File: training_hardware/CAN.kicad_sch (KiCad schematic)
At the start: 7 parts, among them U3 OKI

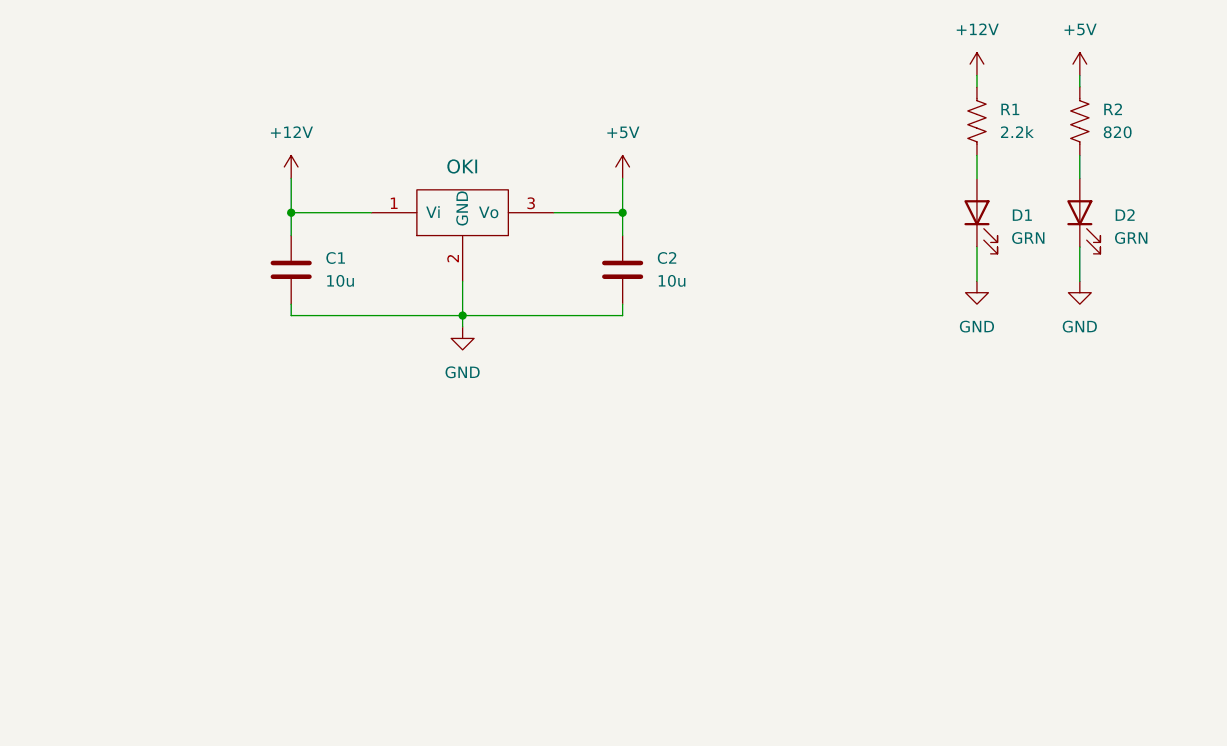
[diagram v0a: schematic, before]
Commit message: Add CAN Transciever
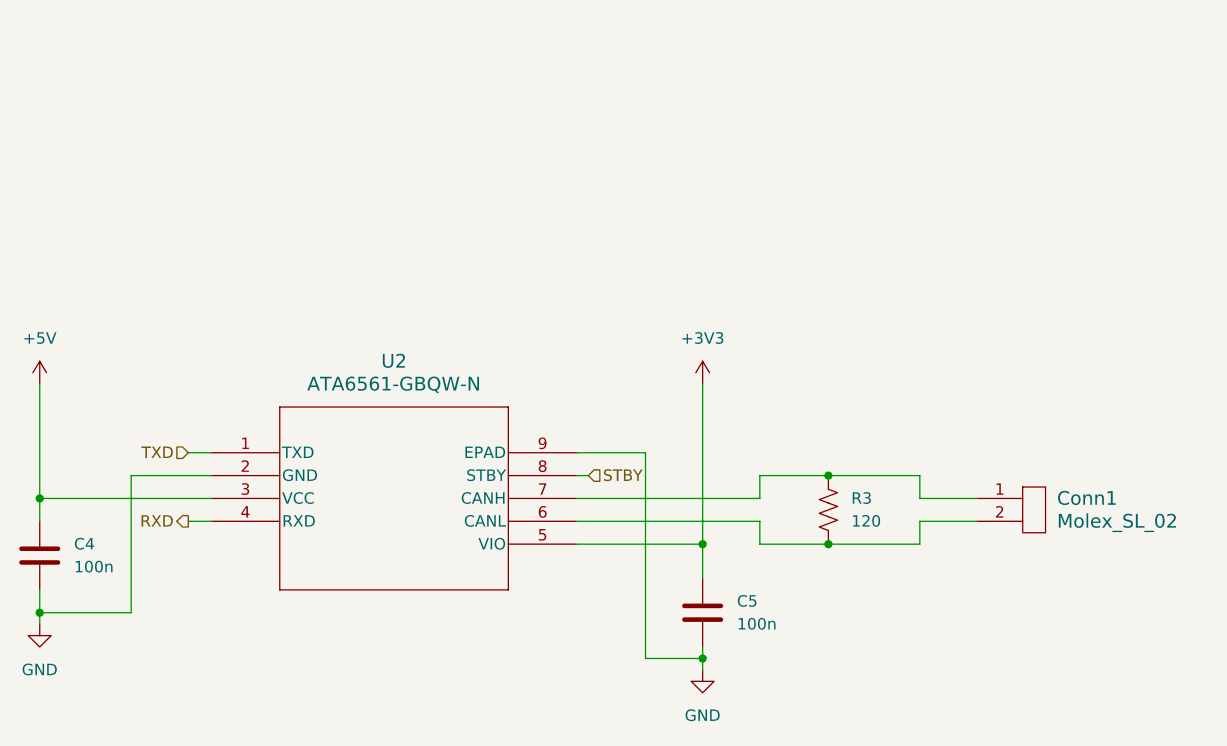
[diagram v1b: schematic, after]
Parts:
- removed C1, C2: 10u, symbol Device:C
- removed D1, D2: GRN, symbol Device:LED
- removed R1: 2.2k, symbol Device:R_US
- removed R2: 820, symbol Device:R_US
- removed U3: OKI, symbol MRDT_Devices:OKI
- added C4, C5: 100n, symbol Device:C
- added Conn1: Molex_SL_02, symbol MRDT_Connectors:Molex_SL_02
- added R3: 120, symbol Device:R_US
- added U2: ATA6561-GBQW-N, VDFN8_3X3_MCH, symbol 2026_training_hardware:ATA6561-GBQW-N
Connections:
- net +5V: now also C4.1, U2.3 (VCC)
- net GND: now also C4.2, C5.2, U2.2 (GND), U2.9 (EPAD)
- new net: Conn1.2, R3.2, U2.6 (CANL)
- new net: Conn1.1, R3.1, U2.7 (CANH)
- new net +3V3: C5.1, U2.5 (VIO)
- new net RXD: U2.4 (RXD)
- new net STBY: U2.8 (STBY)
- new net TXD: U2.1 (TXD)
